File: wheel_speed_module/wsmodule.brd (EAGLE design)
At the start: 21.3 x 48.2 mm, 19 parts, among them T1 BC849, U1 LTC2875XS

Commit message: Version 1.1
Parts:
- added J1: J5MM, jumper:05
- C1: value (none) -> 47u; device eagle-ltspice:C0805 -> eagle-ltspice:C1210
- R1, R2, R3, R4: device eagle-ltspice:R0805 -> eagle-ltspice:R1206
- moved C1_CANL 3.18 mm to (15.9, 20.3)
- moved D2 3.18 mm to (13.3, 29.2)
- moved R4 3.18 mm to (9.53, 27.9)
- moved T1 3.18 mm to (9.53, 33.0)
- moved C2_VCC 2.29 mm to (14.6, 44.5)
- moved C2_SIG 2.29 mm to (6.99, 44.5)
- moved C2_GND 2.29 mm to (10.8, 44.5)
- moved F1 2.01 mm to (14.6, 41.3), turned to 0 degrees
- moved C1 2.01 mm to (10.8, 23.5)
- moved C1_VCC 1.91 mm to (14.6, 2.54)
- moved D1 1.91 mm to (14.6, 35.6)
- moved C1_GND 1.91 mm to (9.53, 2.54)
- moved JP1 1.91 mm to (4.45, 21.6)
- moved R3 1.91 mm to (9.53, 39.4)
- moved R1 1.90 mm to (10.8, 17.8)
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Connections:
- new net 3V3R: J1.2, R4.2
- net 3V3: now also J1.1; no longer R4.2
- net GND: now also JP2.12
- net VCC: no longer C2_VCC.1
- net VIN: now also C2_VCC.1
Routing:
- net GND: track 90.4 -> 1.76 mm
- net 3V3: track 29.7 -> 15.3 mm, vias 2 -> 0
- net 3V3R: track 0.00 -> 13.7 mm
- net CANL: track 28.2 -> 15.4 mm, vias 1 -> 0
- net CAN_TX: track 26.9 -> 38.5 mm, vias 1 -> 0
- net VCC: track 45.0 -> 53.6 mm
- net VIN: track 8.68 -> 16.4 mm
- net DIN1: track 12.2 -> 13.7 mm
- net CANH: track 35.6 -> 36.9 mm, vias 1 -> 0
- net HALL1: track 3.93 -> 4.71 mm
- added copper zone on layer 16, net GND
- removed copper zone on layer 16, net VCC
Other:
- board size 21.3 x 48.2 mm -> 25.1 x 48.2 mm

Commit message: Version 1.2
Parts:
- removed C1_CANH, C1_CANL, C1_GND, C1_VCC, C2_GND, C2_SIG, C2_VCC: WIREPAD1,6/0,8, wirepad:1,6/0,8
- removed D1: BZX84CSMD, diode:TO236
- removed J1: J5MM, jumper:05
- added C3: 100uF, rcl:PANASONIC_D
- added C4: 10uF, rcl:PANASONIC_C
- added CANH, CANL, GND, SGND, SIG, SVCC, VCC: WIREPAD1,6/0,8, wirepad:1,6/0,8
- added IC1: 7805DT, linear:TO252
- moved U1 27.8 mm to (11.9, 38.0), turned to 180 degrees
- moved F1 26.5 mm to (20.2, 15.4), turned to 90 degrees
- moved T1 24.7 mm to (14.6, 57.1), turned to 0 degrees
- moved R4 21.6 mm to (9.53, 49.5)
- moved D2 20.4 mm to (14.6, 49.5)
- moved R3 17.8 mm to (10.3, 57.1)
- moved JP1 17.8 mm to (4.45, 39.4)
- moved JP2 17.8 mm to (19.7, 39.4)
- moved C1 6.25 mm to (13.6, 29.1)
- moved R1 5.67 mm to (14.0, 22.5), turned to 270 degrees
- moved R2 2.44 mm to (9.65, 22.5), turned to 270 degrees
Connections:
- removed net 3V3R: J1.2, R4.2
- new net N$2: C4.+, IC1.2, JP2.1
- net 3V3: now also R4.2; no longer J1.1
- net CANH: now also CANH.1; no longer C1_CANH.1
- net CANL: now also CANL.1; no longer C1_CANL.1
- net GND: now also C3.-, C4.-, GND.1, IC1.3, SGND.1; no longer C1_GND.1, C2_GND.1, D1.A
- net HALL1: now also SIG.1; no longer C2_SIG.1
- net VCC: now also VCC.1; no longer C1_VCC.1
- net VIN: now also C3.+, IC1.1, SVCC.1; no longer C2_VCC.1, D1.C, JP2.1
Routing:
- net N$2: track 0.00 -> 84.3 mm
- net VIN: track 16.4 -> 73.5 mm
- net VCC: track 53.6 -> 5.79 mm
- net 3V3: track 15.3 -> 42.8 mm
- net CAN_TX: track 38.5 -> 14.5 mm
- net CANL: track 15.4 -> 29.8 mm
- net 3V3R: track 13.7 -> 0.00 mm
- net CANH: track 36.9 -> 25.0 mm
- net N$3: track 11.5 -> 18.6 mm
- net CAN_RX: track 11.5 -> 18.1 mm
- net DIN1: track 13.7 -> 18.6 mm
- net GND: track 1.76 -> 0.00 mm
- net HALL1: track 4.71 -> 6.11 mm
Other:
- board size 25.1 x 48.2 mm -> 25.1 x 66 mm

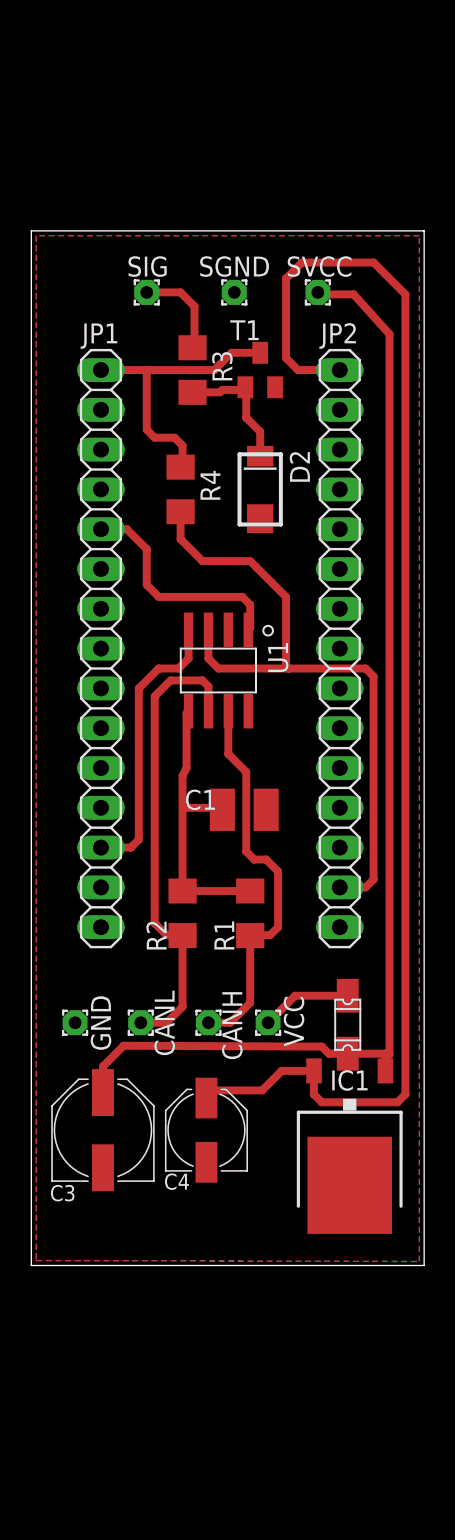
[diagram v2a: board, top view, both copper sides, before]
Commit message: Version 1.3
Two sided assembly. New M8 connectors at each end.
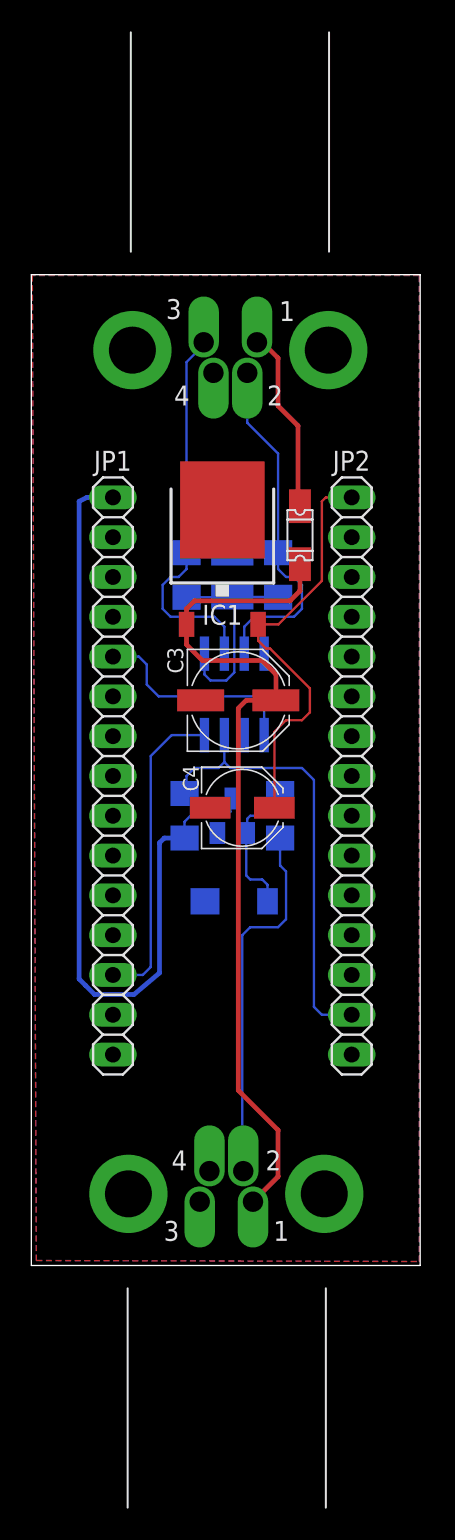
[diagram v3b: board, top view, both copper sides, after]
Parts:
- removed CANH, CANL, GND, SGND, SIG, SVCC, VCC: WIREPAD1,6/0,8, wirepad:1,6/0,8
- added INPUT: M8-718-MALE, SamacSys_Parts:M18-718-MALE
- added OUTPUT: M8-718-FEMALE, SamacSys_Parts:M18-718-FEMALE
- T1: value BC849 -> (none)
- moved IC1 39.0 mm to (12.2, 45.7), turned to 0 degrees
- moved F1 31.4 mm to (17.1, 46.6)
- moved R3 29.0 mm to (15.9, 28.7), flipped to the bottom, turned to 90 degrees
- moved C3 28.8 mm to (13.2, 36.1), turned to 0 degrees
- moved T1 28.5 mm to (12.8, 28.7), flipped to the bottom
- moved D2 26.3 mm to (13.0, 23.2), flipped to the bottom, turned to 0 degrees
- moved R1 21.7 mm to (15.7, 44.1), flipped to the bottom, turned to 90 degrees
- moved R2 21.6 mm to (9.91, 44.1), flipped to the bottom, turned to 90 degrees
- moved R4 20.8 mm to (9.78, 28.7), flipped to the bottom, turned to 90 degrees
- moved C4 20.7 mm to (13.5, 29.2), turned to 0 degrees
- moved C1 15.0 mm to (12.8, 44.1), flipped to the bottom, turned to 90 degrees
- moved JP1 8.16 mm to (5.21, 31.2)
- moved JP2 8.16 mm to (20.4, 31.2)
- moved U1 1.83 mm to (13.0, 36.4), flipped to the bottom, turned to 0 degrees
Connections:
- net N$2 renamed 5V
- net CANH: now also INPUT.P$2; no longer CANH.1
- net CANL: now also INPUT.P$3; no longer CANL.1
- net GND: now also INPUT.L, INPUT.P$4, INPUT.R, OUTPUT.L, OUTPUT.P$4, OUTPUT.R; no longer GND.1, SGND.1
- net HALL1: now also OUTPUT.P$2; no longer SIG.1
- net VCC: now also INPUT.P$1; no longer VCC.1
- net VIN: now also OUTPUT.P$1; no longer SVCC.1
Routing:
- net 5V: track 84.3 -> 27.1 mm
- net DIN1: track 18.6 -> 53.9 mm
- net VIN: track 73.5 -> 55.7 mm
- net HALL1: track 6.11 -> 23.6 mm
- net 3V3: track 42.8 -> 29.0 mm
- net VCC: track 5.79 -> 11.8 mm
- net CANL: track 29.8 -> 24.6 mm
- net N$3: track 18.6 -> 14.5 mm
- net CANH: track 25.0 -> 22.7 mm
- net CAN_RX: track 18.1 -> 20.1 mm
- net N$1: track 8.23 -> 9.68 mm
- net CAN_TX: track 14.5 -> 13.5 mm
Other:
- board size 25.1 x 66 mm -> 24.8 x 63.2 mm
